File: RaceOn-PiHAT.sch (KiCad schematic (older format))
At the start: 75 parts, among them IC1 MIC29302WU, IC10 SN74LVC2G07, IC2 NCP5901B, IC3 NCP5901B, IC4 BD48K60G, IC5 LMR14030, IC6 MPU-9250, IC7 SN74LVC2G07, IC8 SN74LVC2G07, IC9 SN74LVC2G07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

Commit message: Partial fix
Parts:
- removed C14, C16: 220uF, Race On:CAPPM730X435X310L135X240L, symbol Device:CP
- removed C9: 100nF, Race On:CAPC200X125X95L45M, symbol Device:C
- removed IC10: SN74LVC2G07, Race On:SOT23-6P95_280X145L45X37M, symbol RaceOn-PiHAT:SN74LVC2G07
- removed JP2: SolderJumper, Race On:SJ3B12P10X15, symbol RaceOn-PiHAT:SolderJumper
- removed L2: 1uH, Race On:INDM600X600X450L155X490M, symbol Device:L
- removed R16, R17: 3.9k, Race On:RESC200X127X65L40M, symbol Device:R
- removed U5: SPX3819M5-L-1-8, Race On:SOT23-5P95_280X145L45X40M, symbol Regulator_Linear:SPX3819M5-L-1-8
- added JP2, JP5: SolderJumper_2_Bridged, Jumper:SolderJumper-2_P1.3mm_Bridged_Pad1.0x1.5mm, symbol Jumper:SolderJumper_2_Bridged
- LOGO1: footprint Race On:RACEON-LOGO -> Race On:RACEON
- M1: MPN NOT IN OPL -> A2543WV-3P
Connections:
- net ENC_L is gone; now on net BCM16: J2.3 (Pin_3), R18.1
- net ENC_R is gone; now on net BCM26: J2.4 (Pin_4), R19.1
- net +3V3: now also IC7.5 (VCC), IC8.5 (VCC), IC9.5 (VCC), R12.2, R13.2, U1.8 (VCC)
- net +BATT: now also JP2.1 (A), JP5.1 (A)
- net +VSW: now also JP2.2 (B), JP5.2 (B)
- removed net VDD: IC6.8 (VDDIO), IC7.5 (VCC), IC8.5 (VCC), IC9.5 (VCC), R12.2, R13.2, U1.8 (VCC)
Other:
- note removed: "EMI Filter"
- note removed: "SOC Voltage Selector\n1.8V - Jetson Nano\n3.3V - Raspberry Pi"
- moved on the sheet: C11

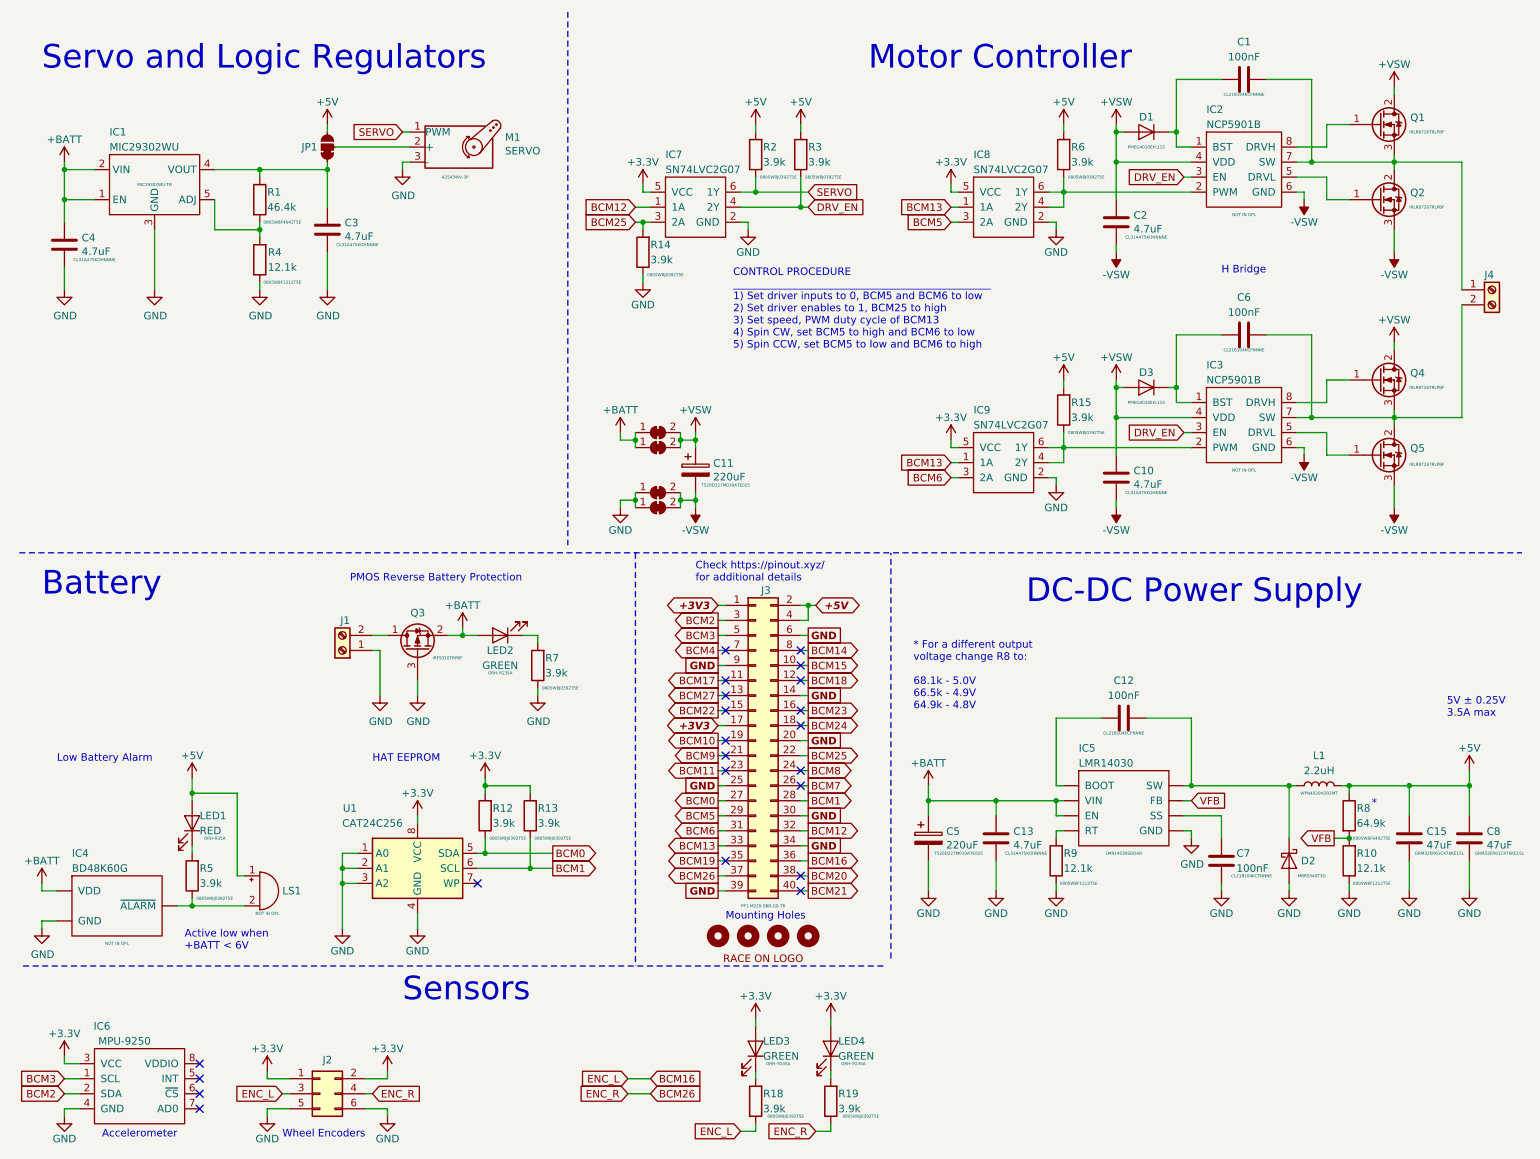
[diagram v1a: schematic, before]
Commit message: Reverded to production board
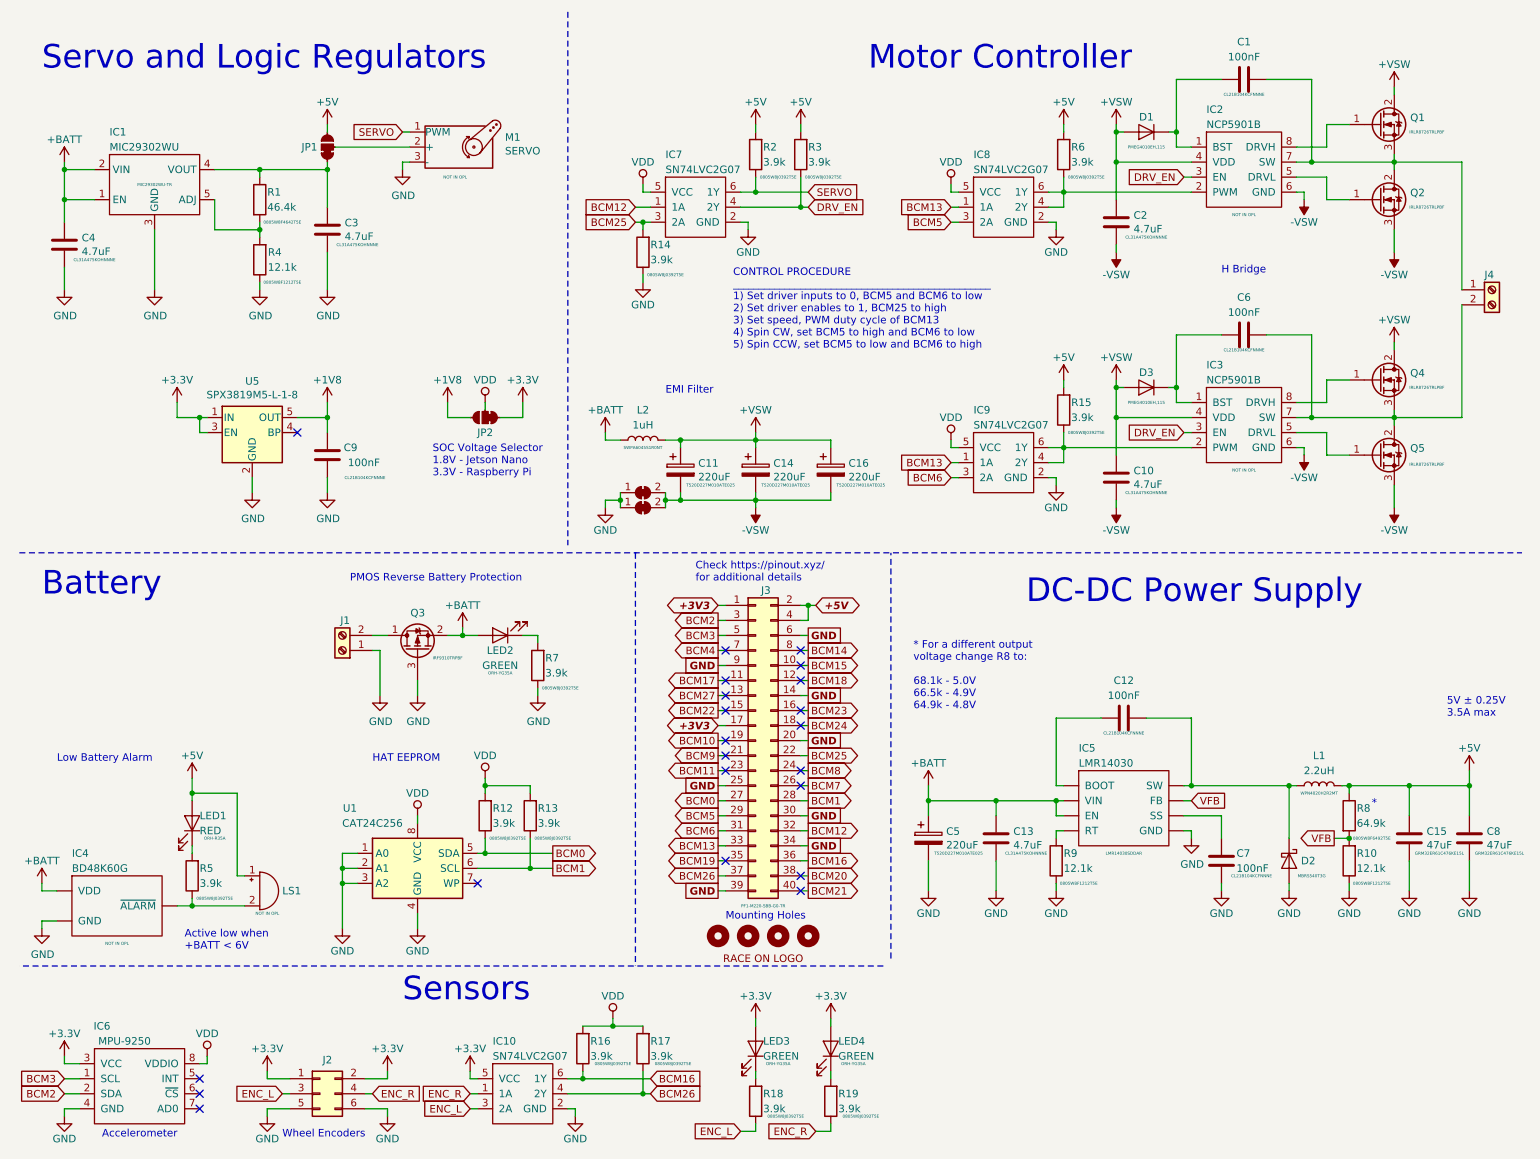
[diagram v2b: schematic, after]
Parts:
- removed JP2, JP5: SolderJumper_2_Bridged, Jumper:SolderJumper-2_P1.3mm_Bridged_Pad1.0x1.5mm, symbol Jumper:SolderJumper_2_Bridged
- added C14, C16: 220uF, Race On:CAPPM730X435X310L135X240L, symbol Device:CP
- added C9: 100nF, Race On:CAPC200X125X95L45M, symbol Device:C
- added IC10: SN74LVC2G07, Race On:SOT23-6P95_280X145L45X37M, symbol RaceOn-PiHAT:SN74LVC2G07
- added JP2: SolderJumper, Race On:SJ3B12P10X15, symbol RaceOn-PiHAT:SolderJumper
- added L2: 1uH, Race On:INDM600X600X450L155X490M, symbol Device:L
- added R16, R17: 3.9k, Race On:RESC200X127X65L40M, symbol Device:R
- added U5: SPX3819M5-L-1-8, Race On:SOT23-5P95_280X145L45X40M, symbol Regulator_Linear:SPX3819M5-L-1-8
- M1: MPN A2543WV-3P -> NOT IN OPL
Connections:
- net +3V3: now also IC10.5 (VCC), JP2.1 (A), U5.1 (IN), U5.3 (EN); no longer IC7.5 (VCC), IC8.5 (VCC), IC9.5 (VCC), R12.2, R13.2, U1.8 (VCC)
- net +BATT: now also L2.2
- net +VSW: now also C14.1, C16.1, L2.1
- net -VSW: now also C14.2, C16.2
- net BCM16: now also IC10.6 (1Y), R16.1; no longer J2.3 (Pin_3), R18.1
- net BCM26: now also IC10.4 (2Y), R17.1; no longer J2.4 (Pin_4), R19.1
- net GND: now also C9.1, IC10.2 (GND), U5.2 (GND)
- net VDD: now reaches IC6.8 (VDDIO)
- net VDD: now also IC7.5 (VCC), IC8.5 (VCC), IC9.5 (VCC), R12.2, R13.2, U1.8 (VCC), JP2.2 (C), R16.2, R17.2
- new net +1V8: C9.2, JP2.3 (B), U5.5 (OUT)
- new net ENC_L: IC10.3 (2A), J2.3 (Pin_3), R18.1
- new net ENC_R: IC10.1 (1A), J2.4 (Pin_4), R19.1
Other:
- note added: "EMI Filter"
- note added: "SOC Voltage Selector\n1.8V - Jetson Nano\n3.3V - Raspberry Pi"
- moved on the sheet: C11

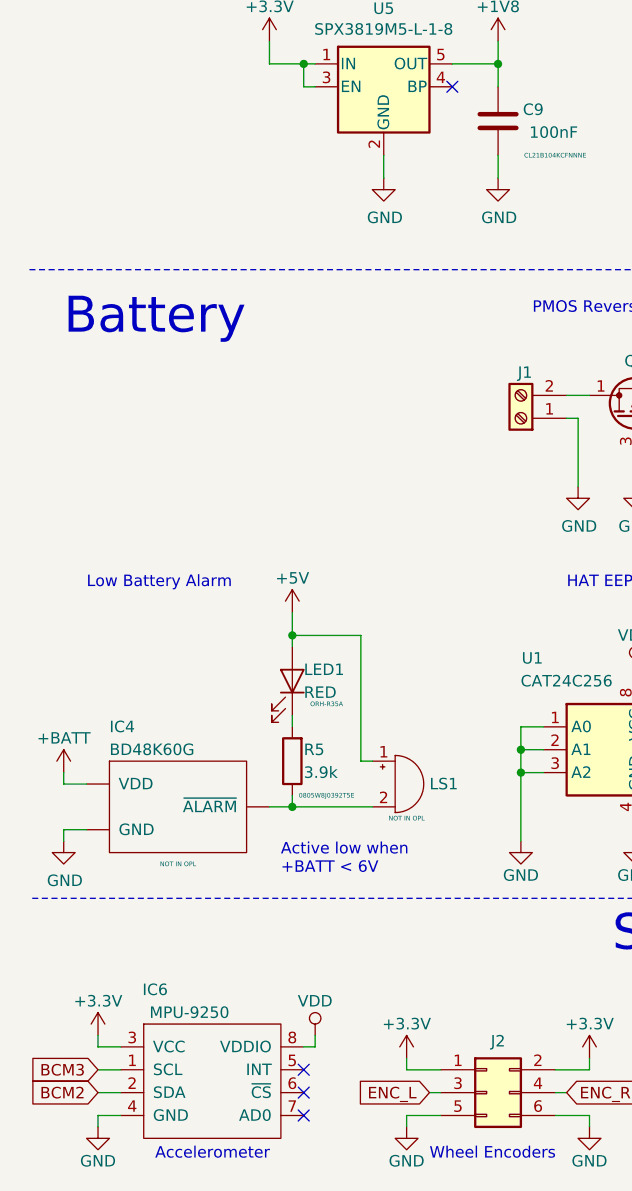
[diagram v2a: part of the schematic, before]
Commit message: Reposition IMU and fix labels
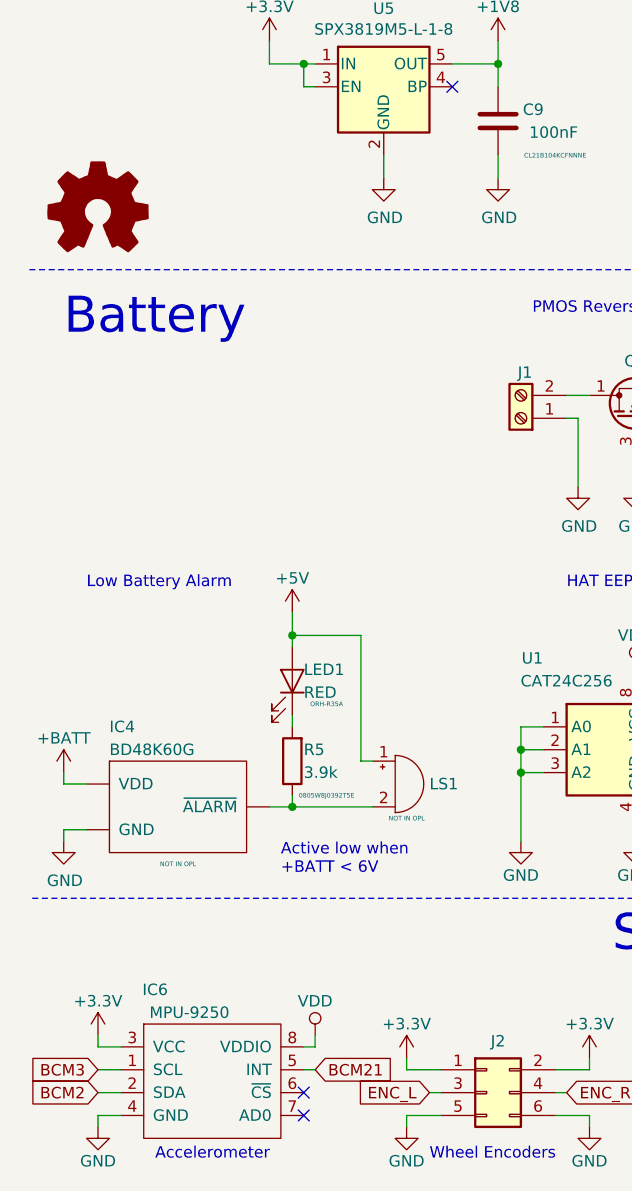
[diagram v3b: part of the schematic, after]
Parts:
- added LOGO2: Logo_Open_Hardware_Small, Symbol:OSHW-Logo2_7.3x6mm_SilkScreen, symbol Graphic:Logo_Open_Hardware_Small
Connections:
- net BCM21: now also IC6.5 (INT)
- no-connect marks 22 -> 21
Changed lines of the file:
@@
 Sheet 1 1
 Title "Race On – Pi HAT"
-Date "2019-08-15"
-Rev "1.2"
+Date "2019-12-22"
+Rev "1.3"
 Comp "University of Southern California"
 Comment1 "Ming Hsieh Department of Electrical and Computer Engineering"
@@
 NoConn ~ 1700 7750
 NoConn ~ 1700 7650
-NoConn ~ 1700 7550
 Wire Wire Line
 	800  7450 900  7450
@@
 NoConn ~ 5200 6100
 NoConn ~ 5700 6300
+$Comp
+L Graphic:Logo_Open_Hardware_Small LOGO2
+U 1 1 5E01E4B3
+P 800 3800
+F 0 "LOGO2" H 800 4075 50  0001 C CNN
+F 1 "Logo_Open_Hardware_Small" H 800 3575 50  0001 C CNN
+F 2 "Symbol:OSHW-Logo2_7.3x6mm_SilkScreen" H 800 3800 50  0001 C CNN
+F 3 "~" H 800 3800 50  0001 C CNN
+	1    800  3800
+	1    0    0    -1
+$EndComp
+Text GLabel 1750 7550 2    50   Input ~ 0
+BCM21
+Wire Wire Line
+	1750 7550 1700 7550
 $EndSCHEMATC

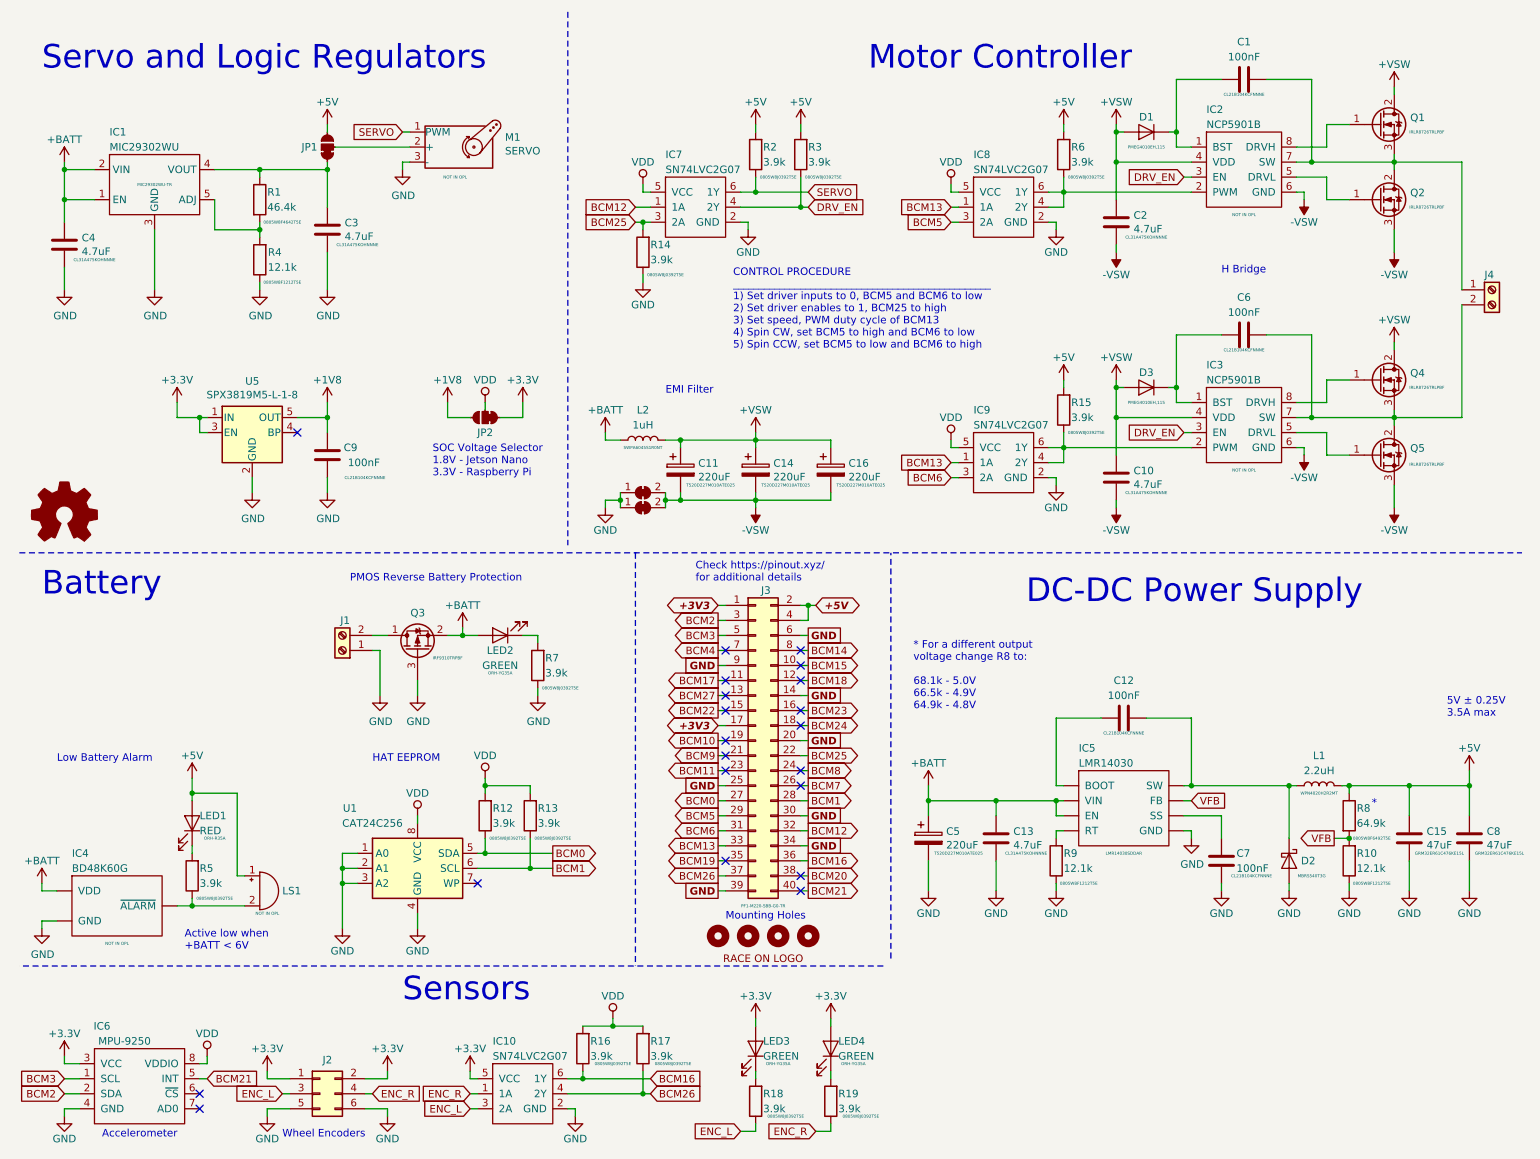
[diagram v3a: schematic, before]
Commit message: Remove EMI filter, replace low ESR caps with ceramic
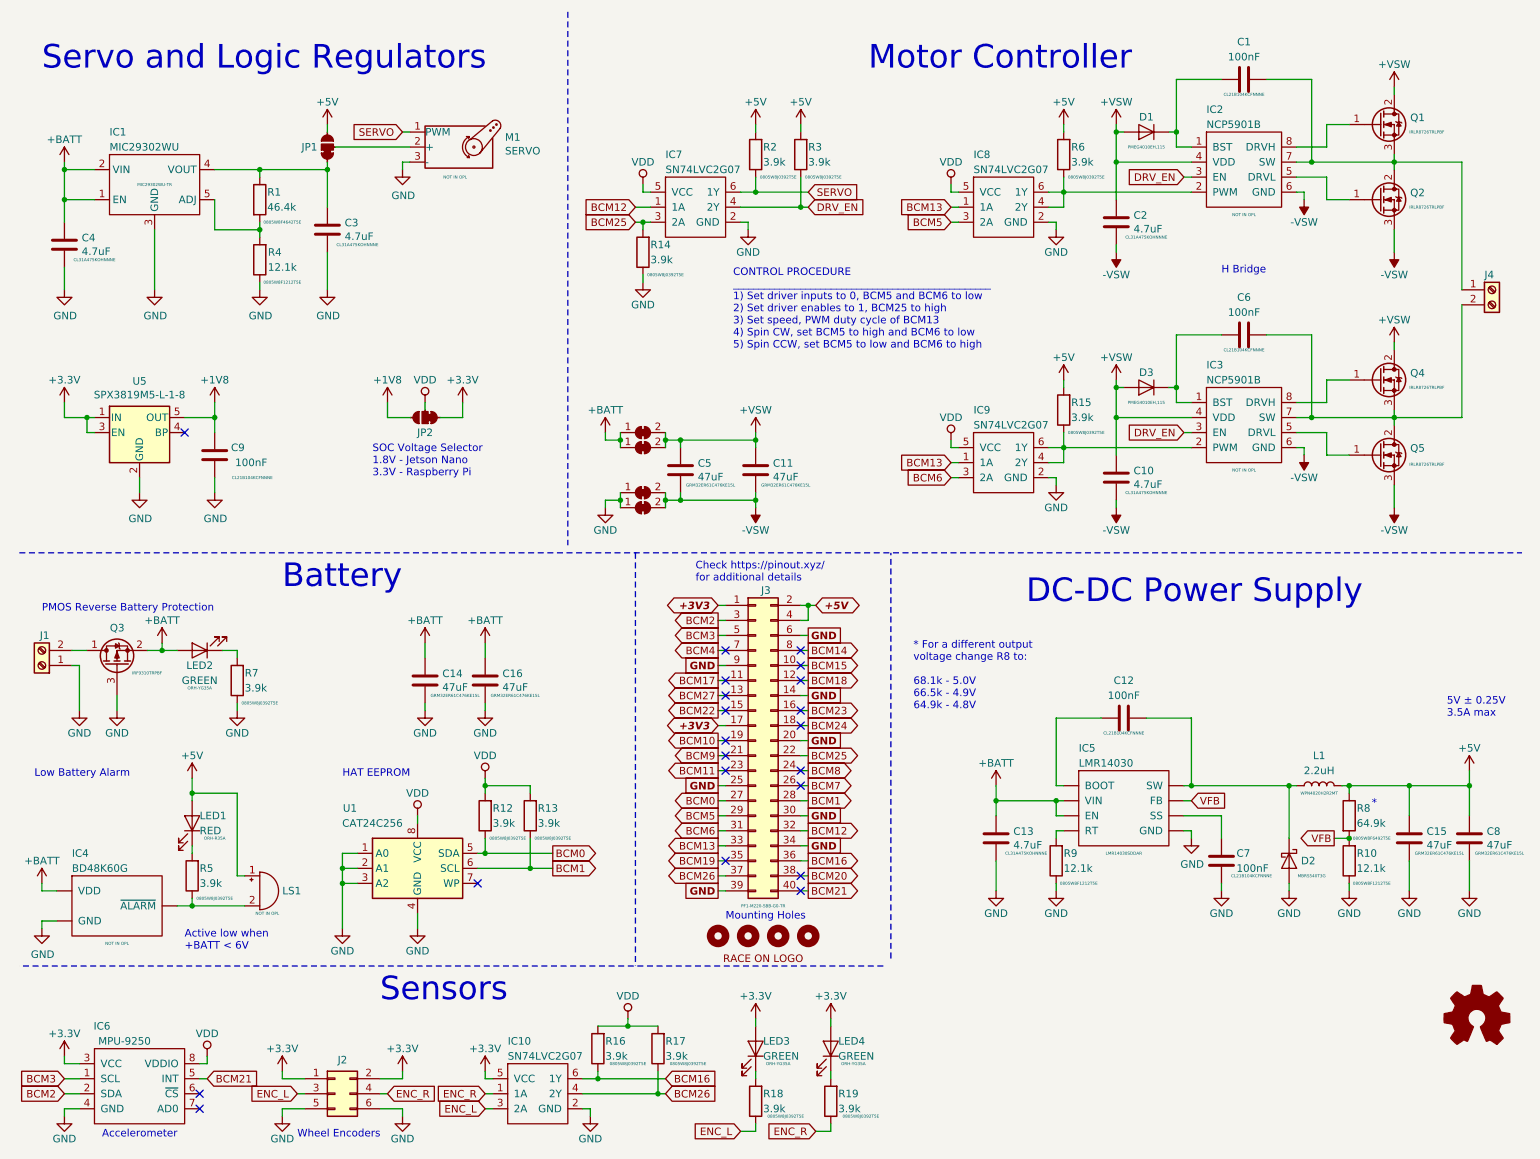
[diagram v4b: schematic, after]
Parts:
- removed C11, C14, C16, C5: 220uF, Race On:CAPPM730X435X310L135X240L, symbol Device:CP
- removed L2: 1uH, Race On:INDM600X600X450L155X490M, symbol Device:L
- added C11, C14, C16, C5: 47uF, Race On:CAPC320X250X270L60M, symbol Device:C
- added JP5, JP6: SolderJumper_2_Bridged, Jumper:SolderJumper-2_P1.3mm_Bridged_Pad1.0x1.5mm, symbol Jumper:SolderJumper_2_Bridged
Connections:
- net +BATT: now also JP3.1 (A), JP4.1 (A), C14.2, C16.2
- net +VSW: now also JP3.2 (B), JP4.2 (B), C11.2, C5.2
- net -VSW: now also C11.1, C5.1, JP5.2 (B), JP6.2 (B); no longer JP3.2 (B), JP4.2 (B)
- net GND: now also C14.1, C16.1, JP5.1 (A), JP6.1 (A); no longer JP3.1 (A), JP4.1 (A)
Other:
- note removed: "EMI Filter"
- moved on the sheet: C9, IC10, J1, J2, JP2, LED2, Q3, R16, R17, R7, U5
